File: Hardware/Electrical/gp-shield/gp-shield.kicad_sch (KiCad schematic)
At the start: 0 parts

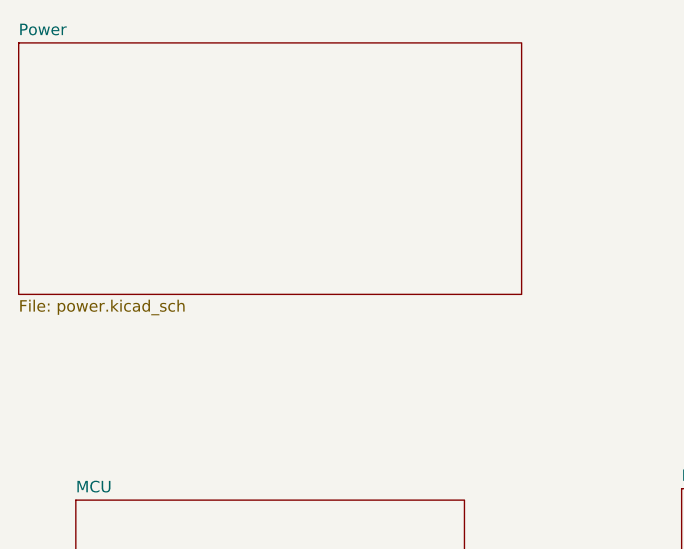
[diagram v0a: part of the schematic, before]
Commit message: Major PCB changes
Added combined footprint for XT60 and terminal port.
Fixed polarity of Batt and PWR_out connectors.
Standardised polarity markers to show negative on white.
Moved Port D and Port B connectors to be inline with existing arduino connectors. Removed extra pins.
Added analogue in-line output.
Adjusted component placement for more space around power supply and GP PB and LED.
Draft version of track routing - incomplete.
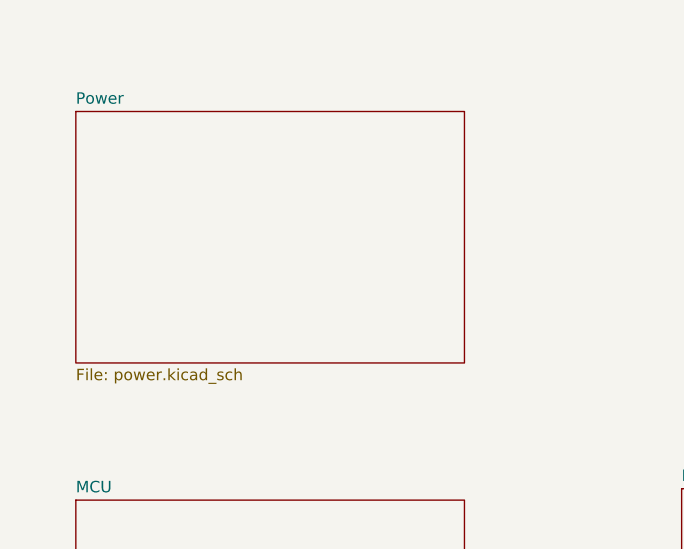
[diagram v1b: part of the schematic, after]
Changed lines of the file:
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@@
     )
   )
-  (sheet (at 63.5 44.45) (size 55.88 27.94) (fields_autoplaced)
+  (sheet (at 69.85 52.07) (size 43.18 27.94) (fields_autoplaced)
     (stroke (width 0.1524) (type solid) (color 0 0 0 0))
     (fill (color 132 0 0 0.5000))
-    (property "Sheet name" "Power" (id 0) (at 63.5 43.7384 0)
+    (property "Sheet name" "Power" (id 0) (at 69.85 51.3584 0)
       (effects (font (size 1.27 1.27)) (justify left bottom))
     )
-    (property "Sheet file" "power.kicad_sch" (id 1) (at 63.5 72.9746 0)
+    (property "Sheet file" "power.kicad_sch" (id 1) (at 69.85 80.5946 0)
       (effects (font (size 1.27 1.27)) (justify left top))
     )
@@
       (reference "#FLG011") (unit 1) (value "PWR_FLAG") (footprint "")
     )
-    (path "/04ed0af3-f777-44ba-9dbd-897161fc6c6a/5e623597-4ad6-40ea-ac7b-b2b6e3074d0d"
-      (reference "#FLG012") (unit 1) (value "PWR_FLAG") (footprint "")
-    )
     (path "/04ed0af3-f777-44ba-9dbd-897161fc6c6a/296e9da8-4b9e-40fe-a893-1f2cd22fe67c"
       (reference "#FLG013") (unit 1) (value "PWR_FLAG") (footprint "")
@@
       (reference "#PWR097") (unit 1) (value "GND") (footprint "")
     )
-    (path "/04ed0af3-f777-44ba-9dbd-897161fc6c6a/1badc8e9-0603-45be-b5c4-ba0d7dec2116"
-      (reference "#PWR098") (unit 1) (value "+5V_GPIO_OUT") (footprint "")
-    )
-    (path "/04ed0af3-f777-44ba-9dbd-897161fc6c6a/1762b05b-cd1a-4dbe-a715-eef4c4fe396b"
-      (reference "#PWR099") (unit 1) (value "GND") (footprint "")
-    )
     (path "/04ed0af3-f777-44ba-9dbd-897161fc6c6a/ebde7290-cfc7-4f6c-88b1-b1bb0604f37c"
       (reference "#PWR0100") (unit 1) (value "+5V_UART_OUT") (footprint "")
@@
       (reference "#PWR0103") (unit 1) (value "GND") (footprint "")
     )
-    (path "/04ed0af3-f777-44ba-9dbd-897161fc6c6a/5dc244d0-8def-4ca8-ad0d-a18c9a7da56e"
+    (path "/04ed0af3-f777-44ba-9dbd-897161fc6c6a/526049a7-af89-4344-96ea-fe97494a2769"
       (reference "#PWR0104") (unit 1) (value "GND") (footprint "")
     )
@@
       (reference "#PWR0119") (unit 1) (value "GND") (footprint "")
     )
-    (path "/04ed0af3-f777-44ba-9dbd-897161fc6c6a/dd31e50d-f5a9-4b68-9f1e-9b1987e5c3b8"
-      (reference "#PWR0120") (unit 1) (value "+3V3_ADC_OUT") (footprint "")
-    )
     (path "/04ed0af3-f777-44ba-9dbd-897161fc6c6a/6ea6e161-a4e6-4bbe-bd1e-24710a16dd70"
       (reference "#PWR0121") (unit 1) (value "GND") (footprint "")
@@
       (reference "#PWR0123") (unit 1) (value "GND") (footprint "")
     )
-    (path "/04ed0af3-f777-44ba-9dbd-897161fc6c6a/dd2c16ed-5ac2-4e1e-a86c-2492abc71e71"
-      (reference "#PWR0124") (unit 1) (value "GND") (footprint "")
-    )
-    (path "/04ed0af3-f777-44ba-9dbd-897161fc6c6a/22d0e7f7-0115-4beb-ad40-dea901a9b8ae"
-      (reference "#PWR0125") (unit 1) (value "GND") (footprint "")
-    )
-    (path "/04ed0af3-f777-44ba-9dbd-897161fc6c6a/993a51e9-9e44-4599-ab2e-82232917df1d"
-      (reference "#PWR0126") (unit 1) (value "+3V3") (footprint "")
-    )
     (path "/0d6e7d94-9779-4ff4-b7a4-a3ca08e2a9ec/5a0cb6cc-8a5f-4380-8550-a4295f2c57ed"
       (reference "A1") (unit 1) (value "Arduino_UNO_R3") (footprint "Module:Arduino_UNO_R3")
@@
       (reference "C19") (unit 1) (value "10u") (footprint "Capacitor_SMD:C_0805_2012Metric_Pad1.18x1.45mm_HandSolder")
     )
-    (path "/04ed0af3-f777-44ba-9dbd-897161fc6c6a/c3c20d4e-566c-4ba9-95ee-6e82f8d29c99"
-      (reference "C20") (unit 1) (value "10u") (footprint "Capacitor_SMD:C_0805_2012Metric_Pad1.18x1.45mm_HandSolder")
-    )
     (path "/04ed0af3-f777-44ba-9dbd-897161fc6c6a/9d2b012f-1472-43a1-9e41-3d87310c258d"
       (reference "C21") (unit 1) (value "100n") (footprint "Capacitor_SMD:C_0805_2012Metric_Pad1.18x1.45mm_HandSolder")
@@
       (reference "C28") (unit 1) (value "100n") (footprint "Capacitor_SMD:C_0805_2012Metric_Pad1.18x1.45mm_HandSolder")
     )
-    (path "/04ed0af3-f777-44ba-9dbd-897161fc6c6a/be5a5189-5ad2-4073-ba9b-f0ca1317e4fe"
-      (reference "C29") (unit 1) (value "100n") (footprint "Capacitor_SMD:C_0805_2012Metric_Pad1.18x1.45mm_HandSolder")
-    )
-    (path "/04ed0af3-f777-44ba-9dbd-897161fc6c6a/b64e5164-cfc8-4506-b8b0-66d2f45f5017"
-      (reference "C30") (unit 1) (value "100n") (footprint "Capacitor_SMD:C_0805_2012Metric_Pad1.18x1.45mm_HandSolder")
-    )
     (path "/74fdf5c2-3151-4dc3-ad40-7d970216f0b1/3fdde0e7-e5a7-4586-8570-92f54d2dc51c"
       (reference "D1") (unit 1) (value "D_Schottky") (footprint "Diode_SMD:D_0805_2012Metric_Pad1.15x1.40mm_HandSolder")
@@
     )
     (path "/74fdf5c2-3151-4dc3-ad40-7d970216f0b1/4b03be13-0852-4c92-907e-559155401823"
-      (reference "J1") (unit 1) (value "XT60/TERM2") (footprint "TerminalBlock:TerminalBlock_bornier-2_P5.08mm")
+      (reference "J1") (unit 1) (value "XT60/TERM2") (footprint "Utility:Combined_TerminalBlock_5.08_XT60_2Row0.2Header")
     )
     (path "/74fdf5c2-3151-4dc3-ad40-7d970216f0b1/8d4b3415-1343-4510-955b-6c9b2bd1ff22"
-      (reference "J2") (unit 1) (value "XT60/TERM2") (footprint "TerminalBlock:TerminalBlock_bornier-2_P5.08mm")
+      (reference "J2") (unit 1) (value "XT60/TERM2") (footprint "Utility:Combined_TerminalBlock_5.08_XT60_2Row0.2Header")
     )
     (path "/0d6e7d94-9779-4ff4-b7a4-a3ca08e2a9ec/02ef3222-dfa9-49c9-ae54-79ba7c7b884d"
@@
       (reference "J9") (unit 1) (value "Conn_01x03") (footprint "Connector_PinHeader_2.54mm:PinHeader_1x03_P2.54mm_Vertical")
     )
-    (path "/04ed0af3-f777-44ba-9dbd-897161fc6c6a/ef6dd26d-e5c8-4243-87a7-39aea8d5d220"
+    (path "/04ed0af3-f777-44ba-9dbd-897161fc6c6a/292a74f7-0773-4d79-8d2e-900daab2fef1"
       (reference "J10") (unit 1) (value "Conn_01x08") (footprint "Connector_PinSocket_2.54mm:PinSocket_1x08_P2.54mm_Vertical")
     )
@@
       (reference "J11") (unit 1) (value "Conn_01x04") (footprint "Connector_Molex:Molex_KK-254_AE-6410-04A_1x04_P2.54mm_Vertical")
     )
-    (path "/04ed0af3-f777-44ba-9dbd-897161fc6c6a/18be47a1-a39f-4625-9d17-16abd2b16f09"
-      (reference "J12") (unit 1) (value "Conn_01x10") (footprint "Connector_PinSocket_2.54mm:PinSocket_1x10_P2.54mm_Vertical")
+    (path "/04ed0af3-f777-44ba-9dbd-897161fc6c6a/622a9326-8c4d-4eff-90a9-bef5d52b6251"
+      (reference "J12") (unit 1) (value "Conn_01x08") (footprint "Connector_PinSocket_2.54mm:PinSocket_1x08_P2.54mm_Vertical")
     )
     (path "/04ed0af3-f777-44ba-9dbd-897161fc6c6a/3aead7ed-d746-4f0c-a3d9-134f56660406"
@@
       (reference "J14") (unit 1) (value "Conn_01x04") (footprint "Connector_Molex:Molex_KK-254_AE-6410-04A_1x04_P2.54mm_Vertical")
     )
+    (path "/04ed0af3-f777-44ba-9dbd-897161fc6c6a/61145355-1808-4a86-8cab-6cf7963bf4e8"
+      (reference "J15") (unit 1) (value "Conn_01x07") (footprint "Connector_PinSocket_2.54mm:PinSocket_1x07_P2.54mm_Vertical")
+    )
     (path "/0d6e7d94-9779-4ff4-b7a4-a3ca08e2a9ec/f6e5709b-0218-4252-ba29-50e3bc1c903d"
       (reference "JP1") (unit 1) (value "Jumper_2_Open") (footprint "Connector_PinHeader_2.54mm:PinHeader_1x02_P2.54mm_Vertical")
@@
       (reference "L7") (unit 1) (value "22n") (footprint "Inductor_SMD:L_0805_2012Metric_Pad1.15x1.40mm_HandSolder")
     )
-    (path "/04ed0af3-f777-44ba-9dbd-897161fc6c6a/4d775e96-4b5f-40f5-8061-0e8cd26bc3ca"
-      (reference "L8") (unit 1) (value "22n") (footprint "Inductor_SMD:L_0805_2012Metric_Pad1.15x1.40mm_HandSolder")
-    )
     (path "/0d6e7d94-9779-4ff4-b7a4-a3ca08e2a9ec/0ab76d73-1a37-48ac-a900-de948eb39b28"

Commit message: Minor cosmetic imporvements
title block and colour theme
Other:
- company: (none) -> University of Tasmania
- title: (none) -> gp-shield
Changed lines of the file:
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@@
 (kicad_sch (version 20211123) (generator eeschema)
   (paper "A4")
+  (title_block
+    (title "gp-shield")
+    (date "2022-12-01")
+    (rev "1")
+    (company "University of Tasmania")
+  )
   (bus (pts (xy 113.03 101.6) (xy 137.16 101.6))
     (stroke (width 0) (type default) (color 0 0 0 0))
